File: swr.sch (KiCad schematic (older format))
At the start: 12 parts, among them T4 12:1, T5 1:12

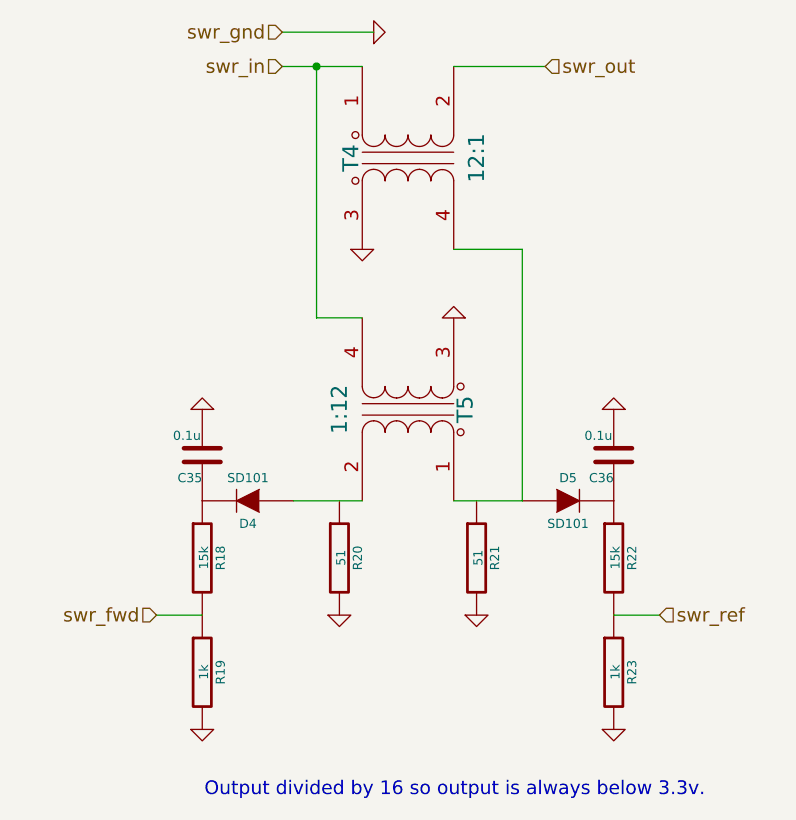
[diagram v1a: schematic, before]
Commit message: All layed out
Several net errors fixed, and some mcu pins reassigned for better layout.
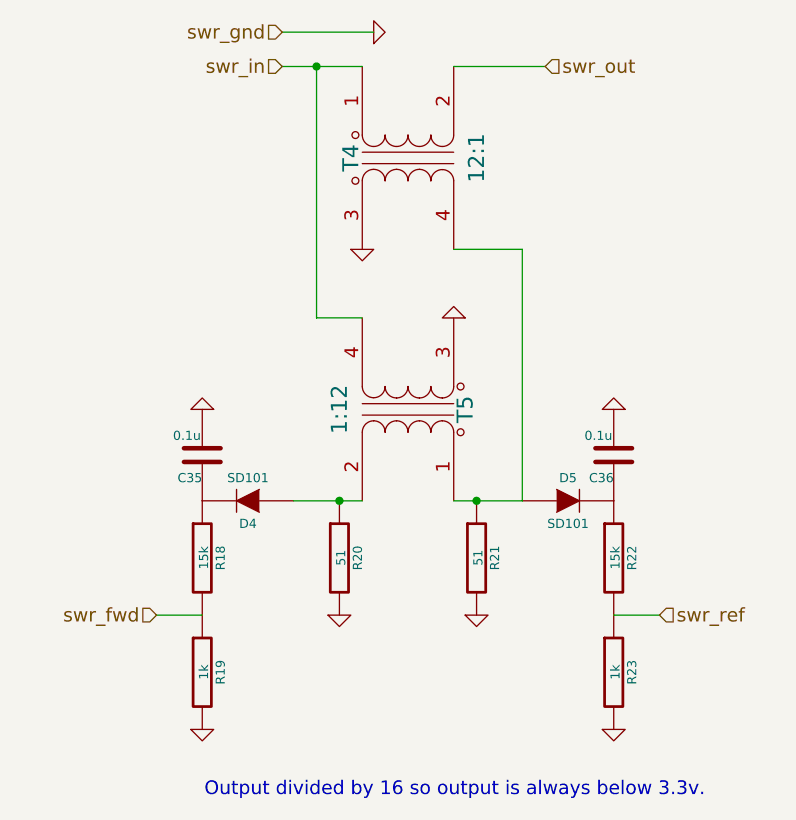
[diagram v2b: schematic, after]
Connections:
- net at D5.1 (A), T4.4 (SB), T5.1 (PA): now also R21.1
- net at D4.1 (A), T5.2 (PB): now also R20.1
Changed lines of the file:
@@
 Text Notes 6450 5750 2    60   ~ 0
 Output divided by 16 so output is always below 3.3v.
+Connection ~ 5450 4450
+Connection ~ 4850 4450
 $EndSCHEMATC

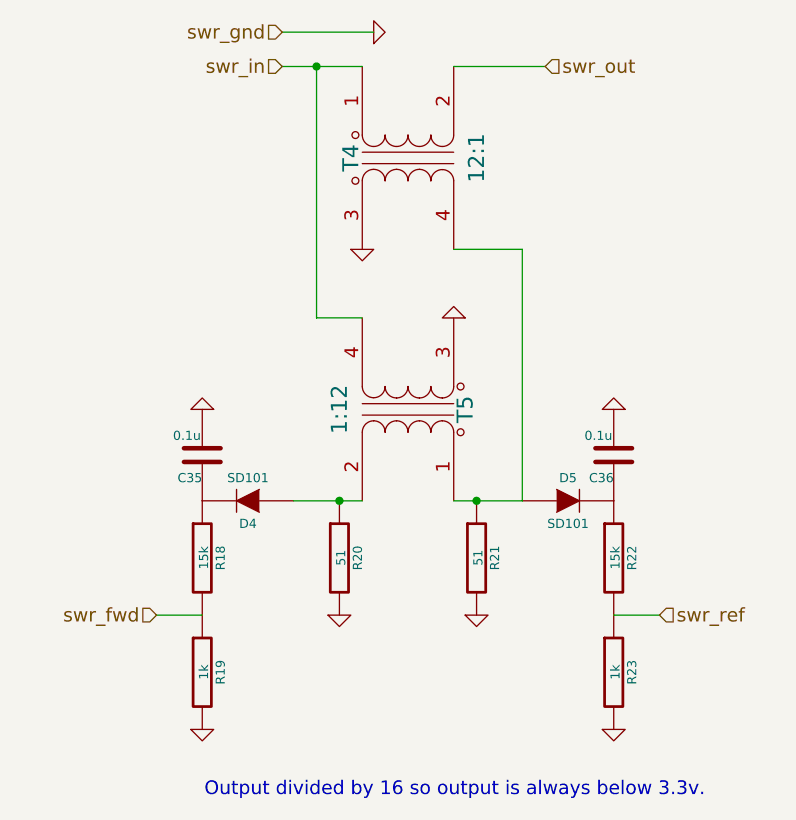
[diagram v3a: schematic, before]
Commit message: Fixes #6: removes SWR measurement voltage divider
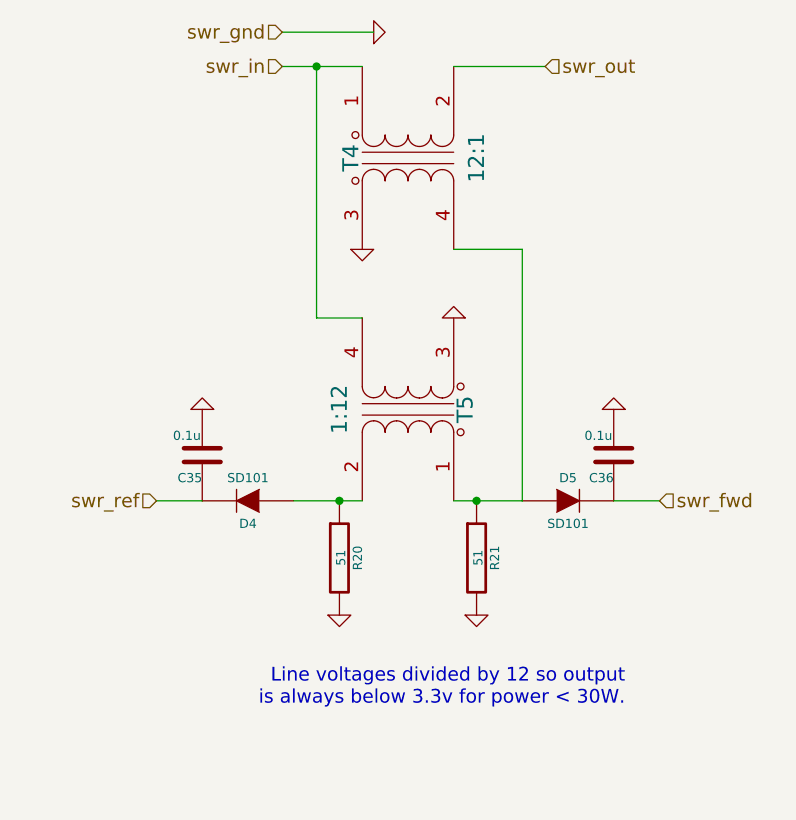
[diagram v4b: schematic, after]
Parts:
- removed R18, R22: 15k, Resistors_SMD:R_1206_HandSoldering, symbol R
- removed R19, R23: 1k, Resistors_SMD:R_1206_HandSoldering, symbol R
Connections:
- net swr_fwd: now also C36.1, D5.2 (K)
- net swr_ref: now also C35.1, D4.2 (K)
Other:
- note added: "Line voltages divided by 12 so output\nis always below 3.3v for power < 30W."
- note removed: "Output divided by 16 so output is always below 3.3v."
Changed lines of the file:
@@
 	-1   0    0    1
 $EndComp
-$Comp
-L R R22
-U 1 1 5471087E
-P 6050 4700
-F 0 "R22" V 6130 4700 40  0000 C CNN
-F 1 "15k" V 6057 4701 40  0000 C CNN
-F 2 "Resistors_SMD:R_1206_HandSoldering" V 5980 4700 30  0001 C CNN
-F 3 "" H 6050 4700 30  0000 C CNN
-	1    6050 4700
-	1    0    0    -1
-$EndComp
-$Comp
-L R R23
-U 1 1 54710890
-P 6050 5200
-F 0 "R23" V 6130 5200 40  0000 C CNN
-F 1 "1k" V 6057 5201 40  0000 C CNN
-F 2 "Resistors_SMD:R_1206_HandSoldering" V 5980 5200 30  0001 C CNN
-F 3 "" H 6050 5200 30  0000 C CNN
-	1    6050 5200
-	1    0    0    -1
-$EndComp
-$Comp
-L R R18
-U 1 1 5471089B
-P 4250 4700
-F 0 "R18" V 4330 4700 40  0000 C CNN
-F 1 "15k" V 4257 4701 40  0000 C CNN
-F 2 "Resistors_SMD:R_1206_HandSoldering" V 4180 4700 30  0001 C CNN
-F 3 "" H 4250 4700 30  0000 C CNN
-	1    4250 4700
-	1    0    0    -1
-$EndComp
-$Comp
-L R R19
-U 1 1 547108A6
-P 4250 5200
-F 0 "R19" V 4330 5200 40  0000 C CNN
-F 1 "1k" V 4257 5201 40  0000 C CNN
-F 2 "Resistors_SMD:R_1206_HandSoldering" V 4180 5200 30  0001 C CNN
-F 3 "" H 4250 5200 30  0000 C CNN
-	1    4250 5200
-	1    0    0    -1
-$EndComp
-$Comp
-L GND #PWR099
-U 1 1 547108D1
-P 4250 5450
-F 0 "#PWR099" H 4250 5450 30  0001 C CNN
-F 1 "GND" H 4250 5380 30  0001 C CNN
-F 2 "" H 4250 5450 60  0000 C CNN
-F 3 "" H 4250 5450 60  0000 C CNN
-	1    4250 5450
-	1    0    0    -1
-$EndComp
-$Comp
-L GND #PWR0100
-U 1 1 547108E5
-P 6050 5450
-F 0 "#PWR0100" H 6050 5450 30  0001 C CNN
-F 1 "GND" H 6050 5380 30  0001 C CNN
-F 2 "" H 6050 5450 60  0000 C CNN
-F 3 "" H 6050 5450 60  0000 C CNN
-	1    6050 5450
-	1    0    0    -1
-$EndComp
 Wire Wire Line
-	6050 4950 6250 4950
+	4250 4450 4050 4450
 Wire Wire Line
-	4250 4950 4050 4950
-Text HLabel 6250 4950 2    60   Input ~ 0
+	6050 4450 6250 4450
+Text HLabel 4050 4450 0    60   Input ~ 0
 swr_ref
-Text HLabel 4050 4950 0    60   Input ~ 0
+Text HLabel 6250 4450 2    60   Input ~ 0
 swr_fwd
-Text Notes 6450 5750 2    60   ~ 0
-Output divided by 16 so output is always below 3.3v.
+Text Notes 6100 5350 2    60   ~ 0
+Line voltages divided by 12 so output\nis always below 3.3v for power < 30W.
 Connection ~ 5450 4450
 Connection ~ 4850 4450
